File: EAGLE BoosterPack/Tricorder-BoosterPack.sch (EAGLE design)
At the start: 16 parts

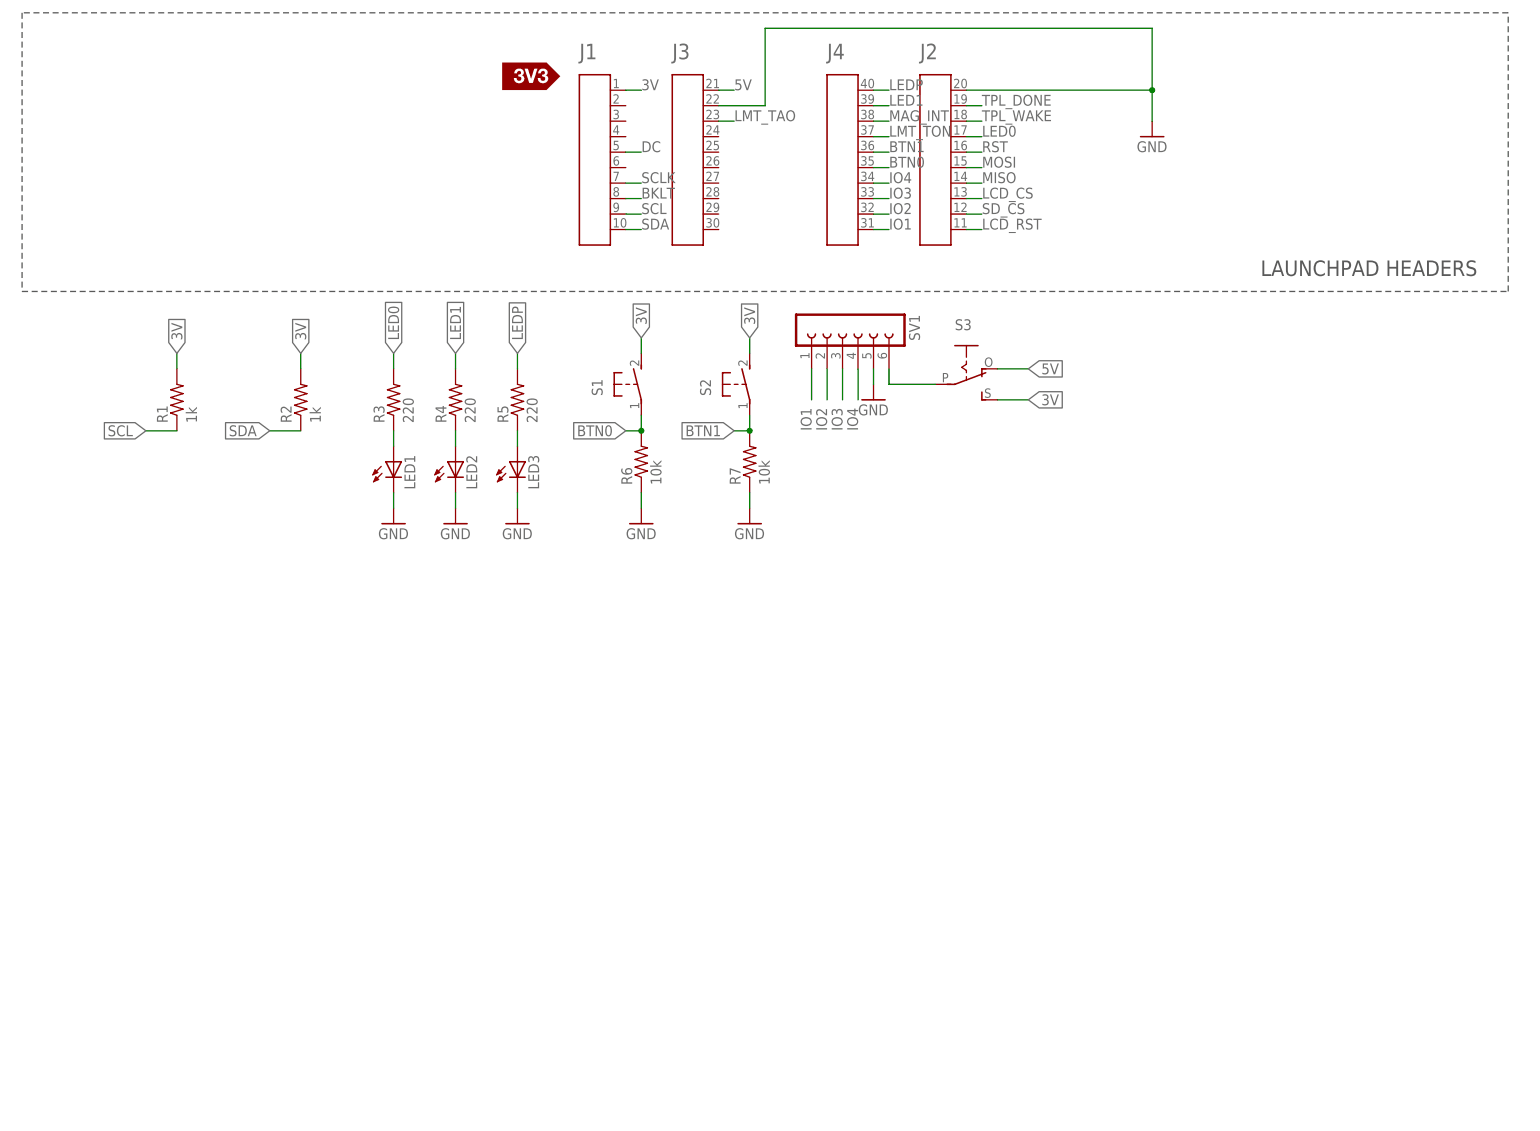
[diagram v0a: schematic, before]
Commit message: SCH/BRD update, Init firmware
Added 4 main sensors to schematic and PMOD, buttons, LEDs, necessary
peripheral components.

Initial firmware release.
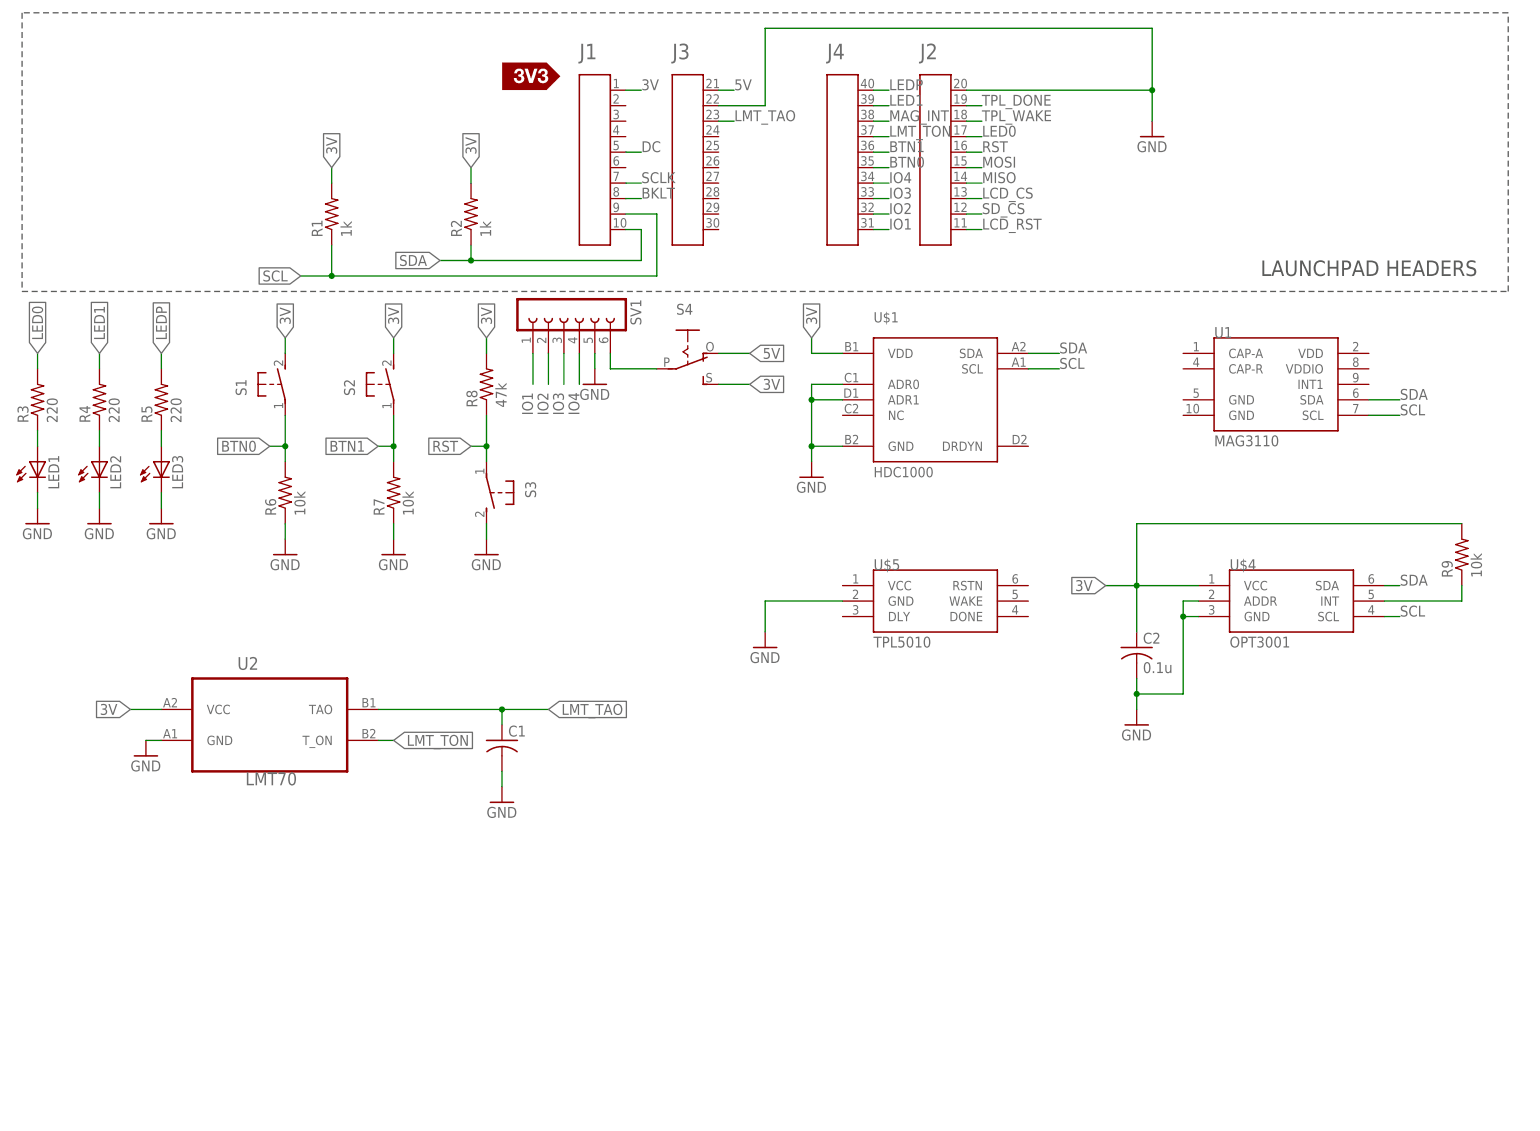
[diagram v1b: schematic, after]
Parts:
- added C1: (no value), adafruit:C-USC0603
- added C2: 0.1u, adafruit:C-USC0603
- added R8: 47k, resistor:R-US_R0603
- added R9: 10k, resistor:R-US_R0603
- added S4: (no value), adafruit:EG1218S
- added U$1: HDC1000, Fra:HDC1000
- added U$4: OPT3001, OPT3001:OPT3001
- added U$5: TPL5010, LPT5010:TPL5010TPL5010
- added U1: MAG3110, SparkFun-Sensors:MAG3110
- added U2: LMT70LMT70, LMT70:LMT70LMT70
- S3: device adafruit:EG1218S -> adafruit:31-XX
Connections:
- new net N$5: R9.1, U$4.INT
- new net N$6: U2.VCC
- net 3V: now also C2.1, R8.2, R9.2, S4.S, U$1.VDD, U$4.VCC; no longer S3.S
- net 5V: now also S4.O; no longer S3.O
- net GND: now also C1.2, C2.2, S3.S, U$1.ADR0, U$1.ADR1, U$1.GND, U$4.ADDR, U$4.GND, U$5.GND, U2.GND
- net LMT_TAO: now also C1.1, U2.TAO
- net LMT_TON: now also U2.T_ON
- net N$4: now also S4.P; no longer S3.P
- net RST: now also R8.1, S3.P
- net SCL: now also U$1.SCL, U$4.SCL, U1.SCL
- net SDA: now also U$1.SDA, U$4.SDA, U1.SDA
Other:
- moved on the sheet: LED1, LED2, LED3, R1, R2, R3, R4, R5, R6, R7, S1, S2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

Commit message: Hardware Lock
Hardware design locked for TI review and approval.  3D CAD files
updated to reflect new PCB dimensions.
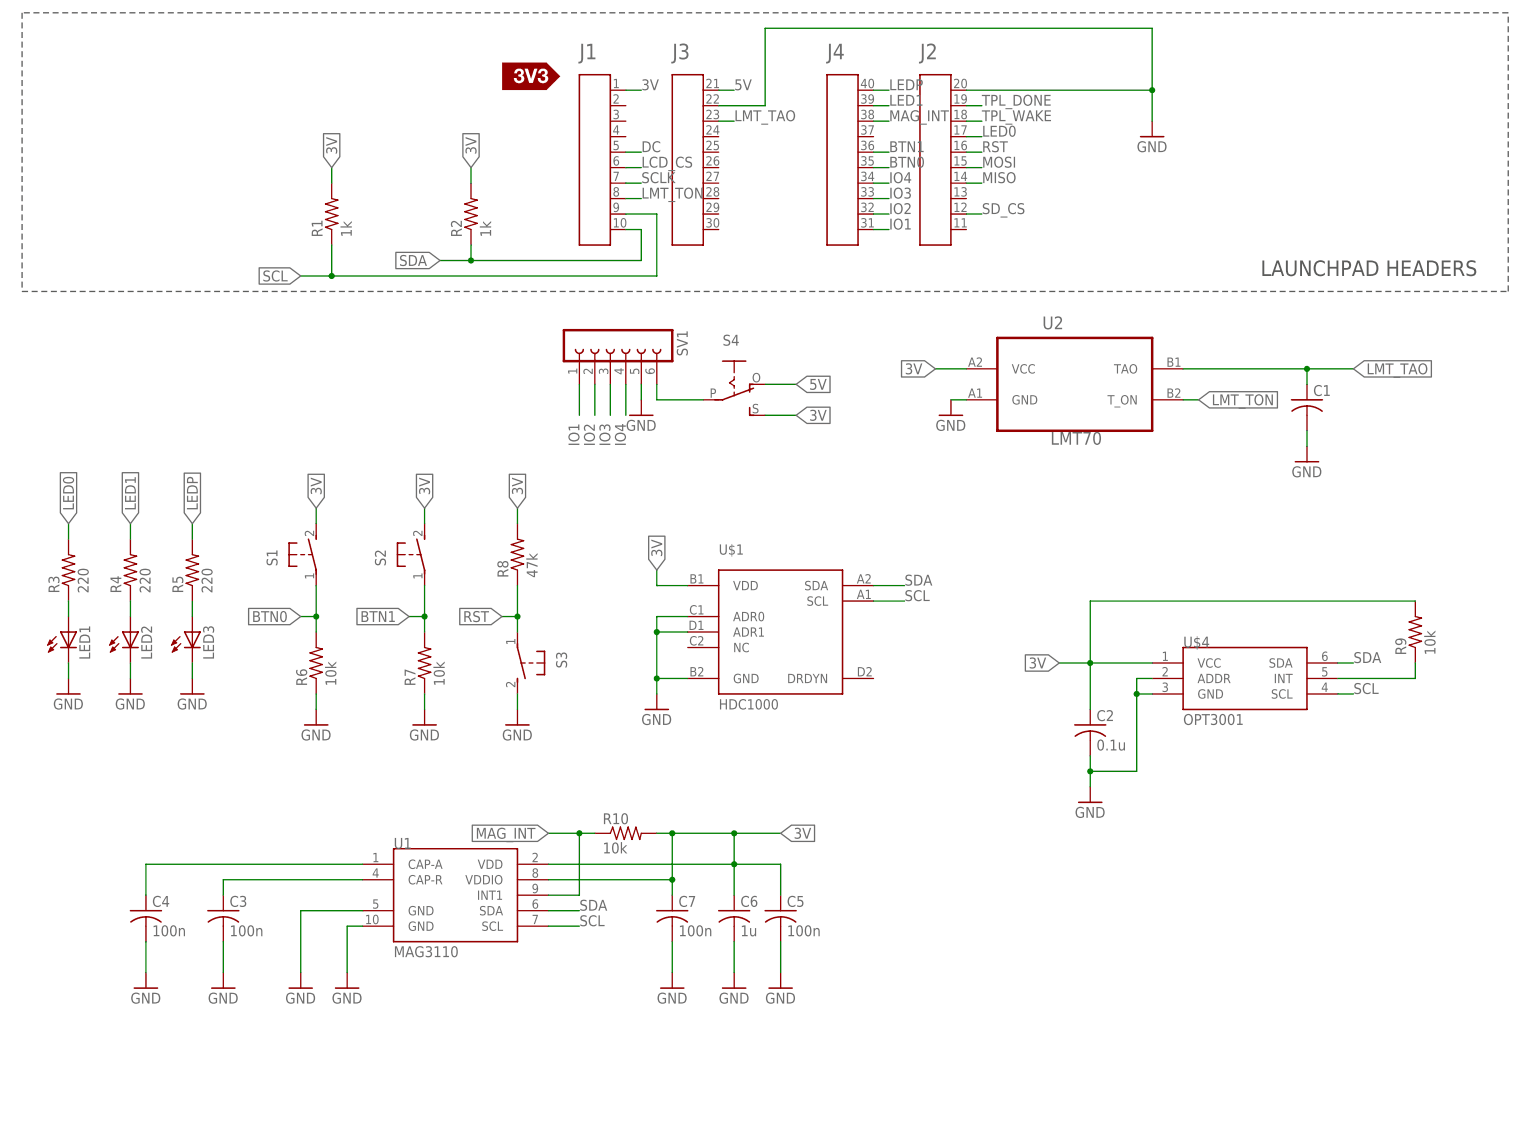
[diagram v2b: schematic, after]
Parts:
- removed U$5: TPL5010, LPT5010:TPL5010TPL5010
- added C3, C4, C5, C7: 100n, adafruit:C-USC0603
- added C6: 1u, adafruit:C-USC0603
- added R10: 10k, resistor:R-US_R0603
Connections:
- removed net BKLT: A1.P$8
- removed net LCD_RST: A1.P$11
- new net N$11: C5.1, C6.1, C7.1, R10.2, U1.VDD, U1.VDDIO
- new net N$8: C3.1, U1.CAP-R
- new net N$9: C4.1, U1.CAP-A
- net GND: now also C3.2, C4.2, C5.2, C6.2, C7.2, U1.GND@10, U1.GND@5; no longer U$5.GND
- net LCD_CS: now also A1.P$6; no longer A1.P$13
- net LMT_TON: now also A1.P$8; no longer A1.P$37
- net MAG_INT: now also R10.1, U1.INT1
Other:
- moved on the sheet: C1, C2, LED1, LED2, LED3, R3, R4, R5, R6, R7, R8, R9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

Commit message: LMP91000 and Alphasense O2-A1 Sensor
Reconfigured board to include a TI LMP91000 gas sensor I2C interface
chip and placeholder for Alphasense O2-A1 oxygen sensor
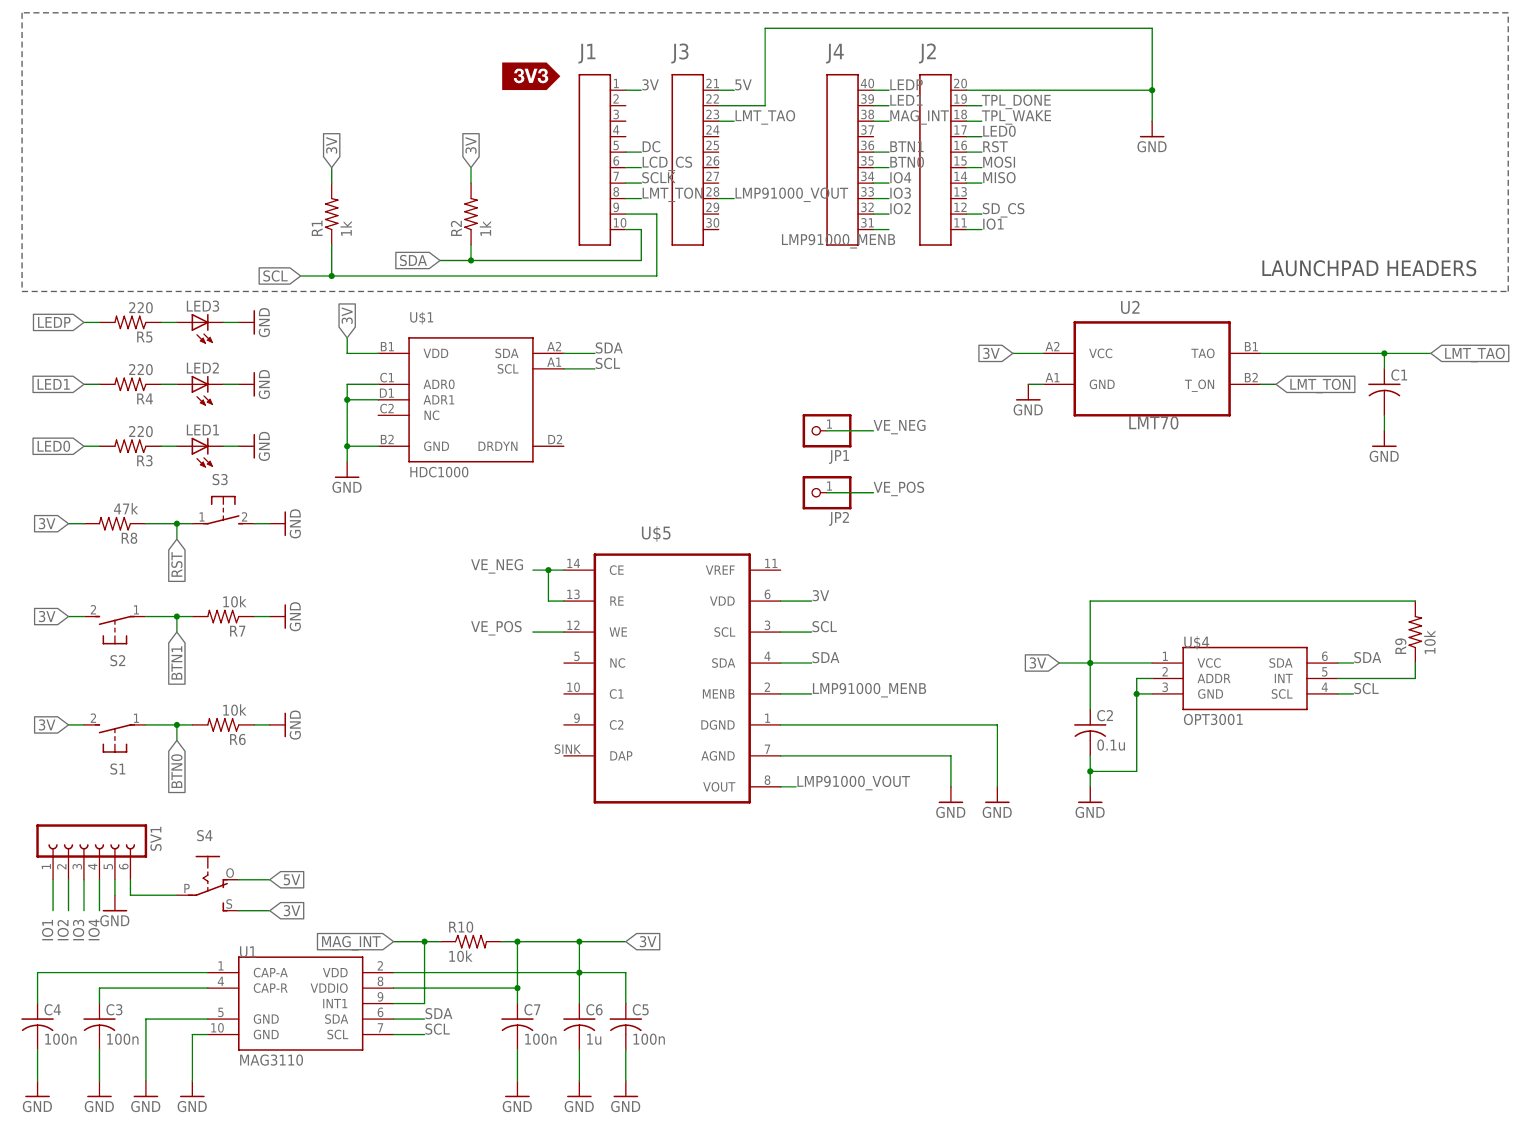
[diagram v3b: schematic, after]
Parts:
- added JP1, JP2: (no value), adafruit:PINHD-1X1CB
- added U$5: LMP91000, LMP91000:LMP91000
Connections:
- new net LMP91000_MENB: A1.P$31, U$5.MENB
- new net LMP91000_VOUT: A1.P$28, U$5.VOUT
- new net VE_NEG: JP1.1, U$5.CE, U$5.RE
- new net VE_POS: JP2.1, U$5.WE
- net 3V: now also U$5.VDD
- net GND: now also U$5.AGND, U$5.DGND
- net IO1: now also A1.P$11; no longer A1.P$31
- net SCL: now also U$5.SCL
- net SDA: now also U$5.SDA
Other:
- moved on the sheet: C1, C3, C4, C5, C6, C7, LED1, LED2, LED3, R10, R3, R4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

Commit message: O2 Sensor Moved Offboard
Replace onboard O2 sensor with header pins to allow for off board
placement of sensor. Eagle files revised as well as documentation files.
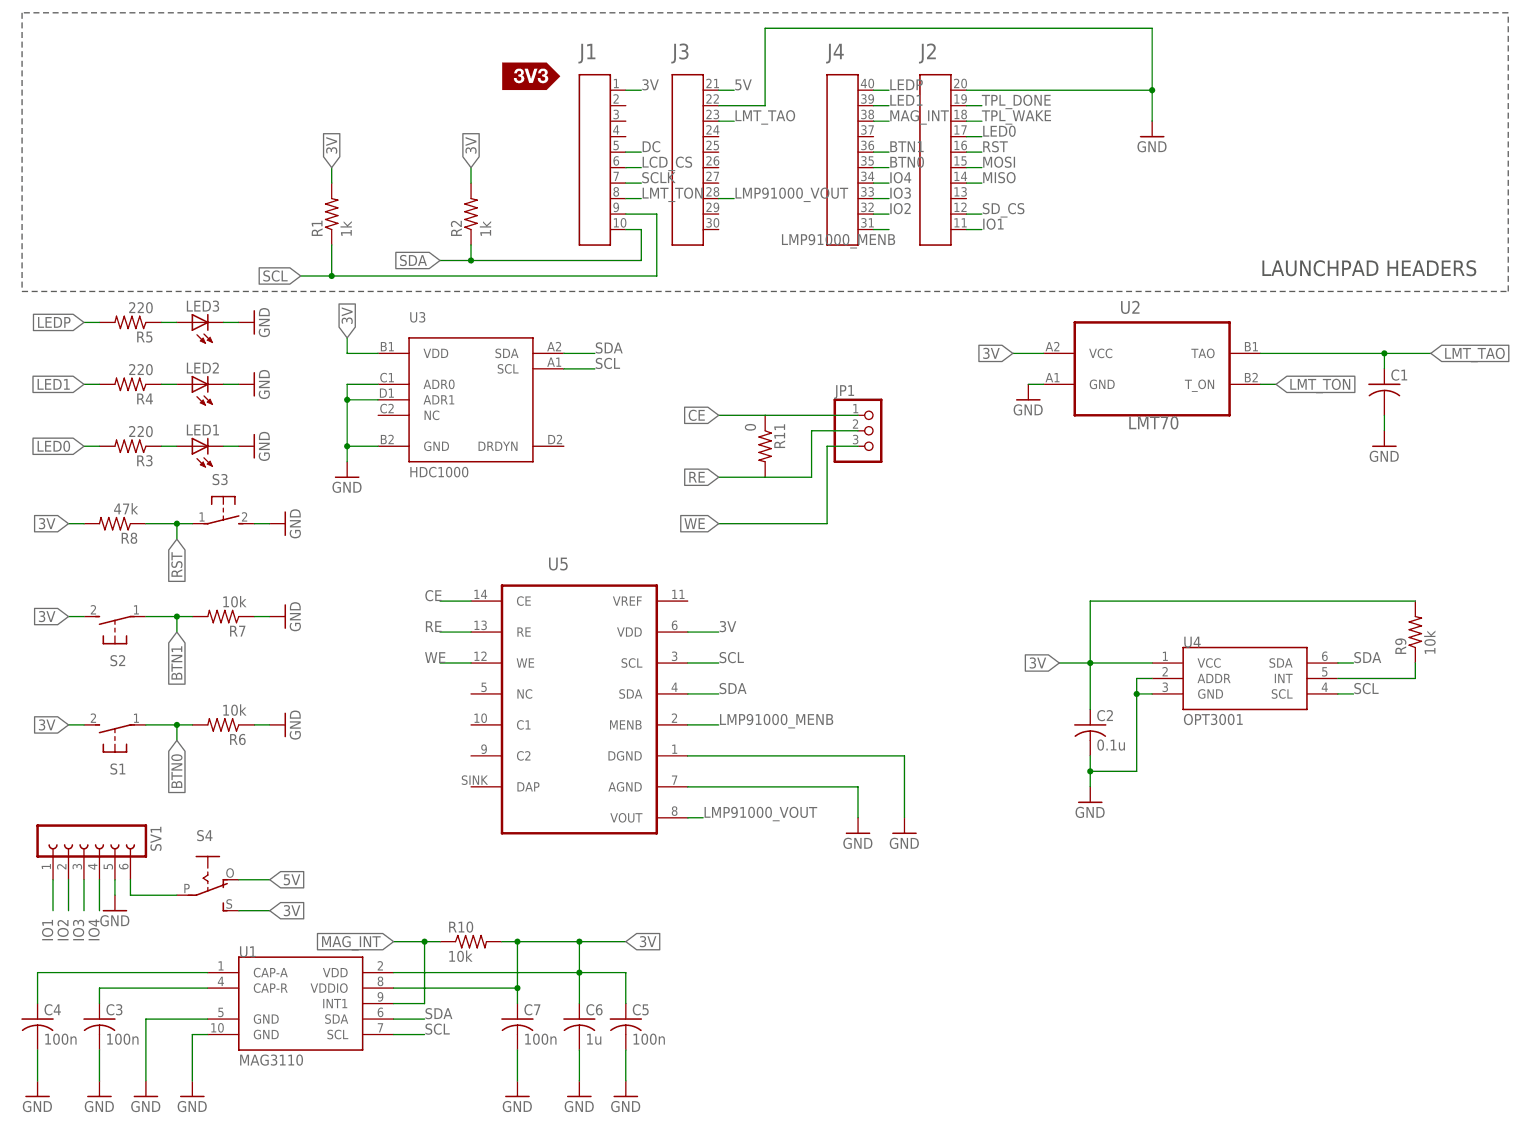
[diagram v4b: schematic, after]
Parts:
- removed JP2: (no value), adafruit:PINHD-1X1CB
- removed U$5: LMP91000, LMP91000:LMP91000
- added R11: 0, resistor:R-US_R0603
- added U5: LMP91000, LMP91000:LMP91000
- JP1: device adafruit:PINHD-1X1CB -> adafruit:PINHD-1X3CB
- renumbered U$1 to U3, U$4 to U4
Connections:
- removed net VE_NEG: JP1.1, U$5.CE, U$5.RE
- removed net VE_POS: JP2.1, U$5.WE
- new net CE: JP1.1, R11.1, U5.CE
- new net RE: JP1.2, R11.2, U5.RE
- new net WE: JP1.3, U5.WE
- net 3V: now also U5.VDD; no longer U$5.VDD
- net GND: now also U5.AGND, U5.DGND; no longer U$5.AGND, U$5.DGND
- net LMP91000_MENB: now also U5.MENB; no longer U$5.MENB
- net LMP91000_VOUT: now also U5.VOUT; no longer U$5.VOUT
- net SCL: now also U5.SCL; no longer U$5.SCL
- net SDA: now also U5.SDA; no longer U$5.SDA
